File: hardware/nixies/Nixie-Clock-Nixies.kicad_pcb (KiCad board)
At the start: 2 copper layers, 25 parts, among them J1 Nixies-Connector

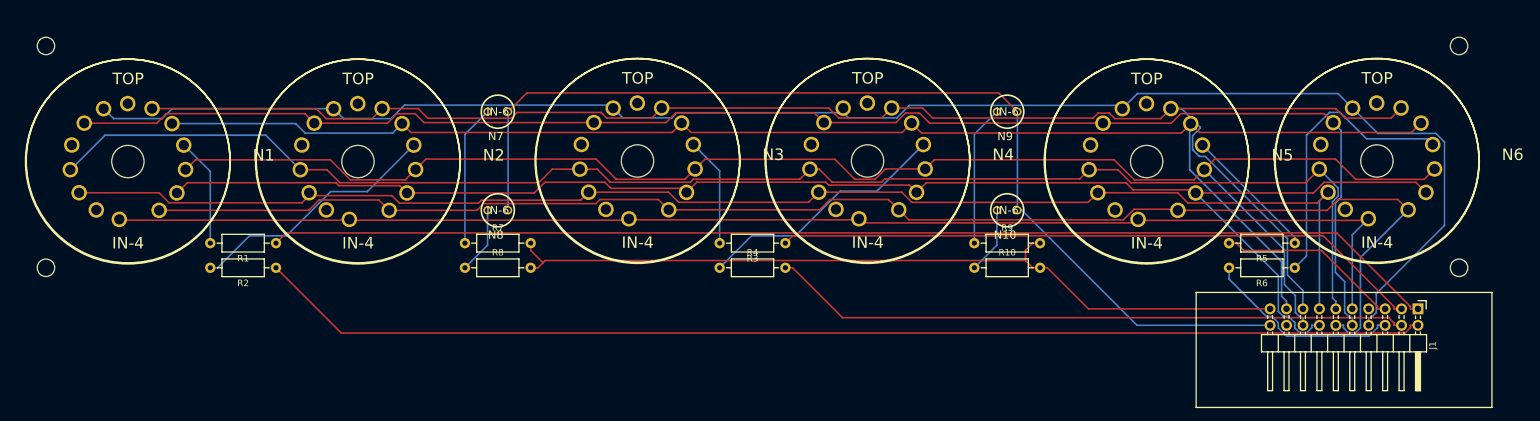
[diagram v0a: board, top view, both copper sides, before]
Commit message: Shrink pcbs
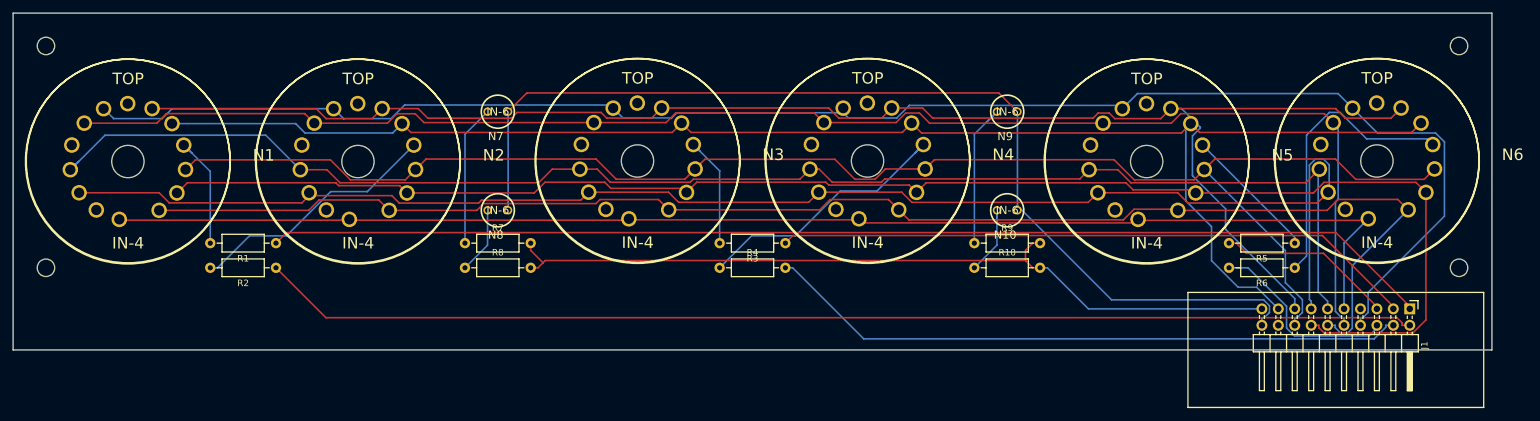
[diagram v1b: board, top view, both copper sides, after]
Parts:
- moved J1 1.27 mm to (236.2, 64.8)
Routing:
- net /c5: track 218.3 -> 231.3 mm
- net /c6: track 232.1 -> 239.1 mm
- net /c9: track 233.9 -> 237.8 mm
- net /dc: track 158.0 -> 160.7 mm
- net Net-(N9-PadA): track 21.8 -> 24.2 mm
- net Net-(N10-PadA): track 10.3 -> 12.4 mm
- net /c3: track 227.5 -> 229.5 mm
- net Net-(N1-PadA3): track 16.8 -> 18.6 mm
- net Net-(N4-PadA3): track 39.4 -> 41.1 mm
- net /a2: track 181.4 -> 179.7 mm
- net Net-(N3-PadA3): track 16.9 -> 18.4 mm
- net /c0: track 250.7 -> 252.0 mm
- net /da: track 126.0 -> 124.7 mm
- net /a4: track 99.1 -> 100.2 mm
- net /c7: track 242.8 -> 241.7 mm
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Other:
- board outline added: 228.6 x 52.1 mm
